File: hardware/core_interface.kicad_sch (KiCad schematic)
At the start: 2 parts, among them J90 Core_LGA, J91 Core_LGA

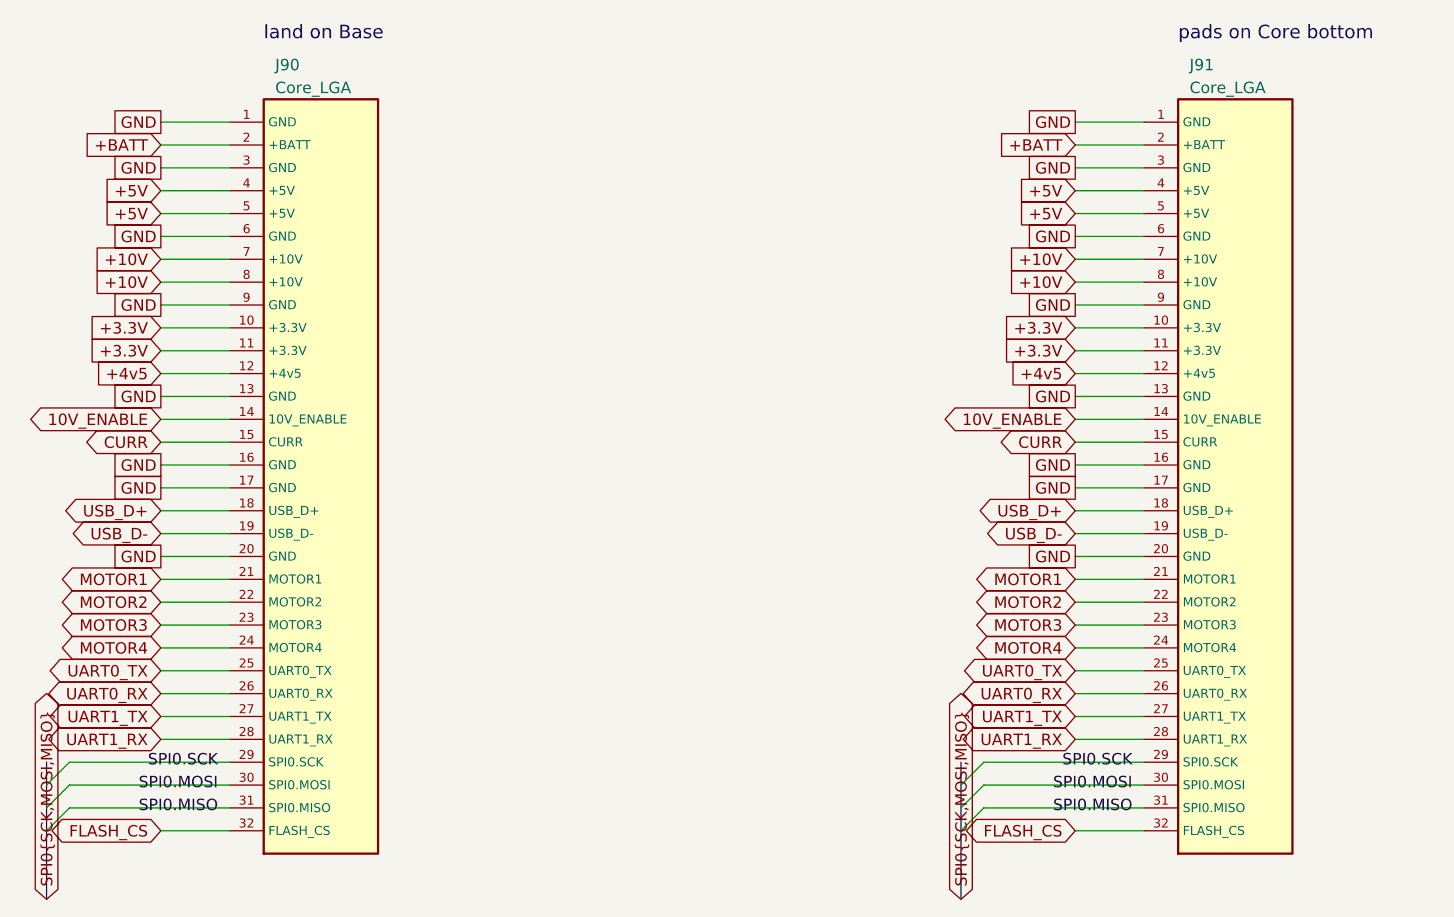
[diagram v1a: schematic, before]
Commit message: OpenAIO: LGA pins from Stan's marker test points, 30 pads, J90/J91 regenerated and placed
lga_gen.py --from-base reads the marker test points on the Base (position +
net) into its pin table and generates footprints, symbol and interface
sheet; lga_apply.py replaces the markers with J90 at the pattern centre and
J91 on the Core, marks the marker symbols exclude-from-board and adds the
LED_STRIP global label on the root (it now crosses the LGA). Plugin update
assigned all 30 pad nets on both boards.

Co-Authored-By: Claude Fable 5 <noreply@anthropic.com>
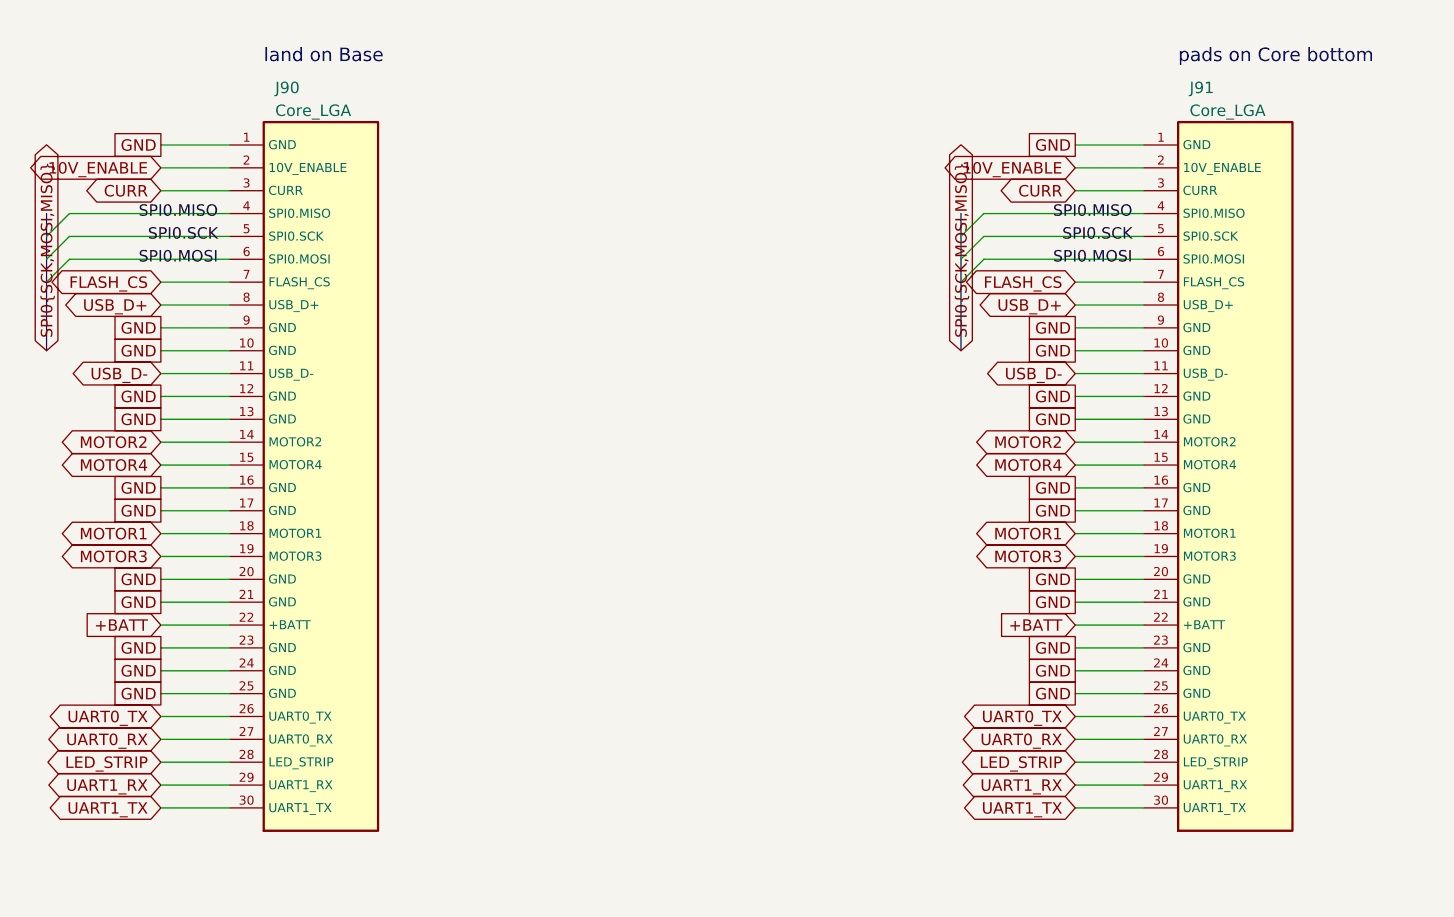
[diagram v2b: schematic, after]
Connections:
- net +4v5 is gone; now on net GND: J90.12 (GND), J91.12 (GND)
- net +BATT: now also J90.22 (+BATT), J91.22 (+BATT); no longer J90.2 (+BATT), J91.2 (+BATT)
- net 10V_ENABLE: now also J90.2 (10V_ENABLE), J91.2 (10V_ENABLE); no longer J90.14 (10V_ENABLE), J91.14 (10V_ENABLE)
- net CURR: now also J90.3 (CURR), J91.3 (CURR); no longer J90.15 (CURR), J91.15 (CURR)
- net FLASH_CS: now also J90.7 (FLASH_CS), J91.7 (FLASH_CS); no longer J90.32 (FLASH_CS), J91.32 (FLASH_CS)
- net GND: now also J90.10 (GND), J90.21 (GND), J90.23 (GND), J90.24 (GND), J90.25 (GND), J91.10 (GND), J91.21 (GND), J91.23 (GND), J91.24 (GND), J91.25 (GND); no longer J90.3 (GND), J90.6 (GND), J91.3 (GND), J91.6 (GND)
- net MOTOR1: now also J90.18 (MOTOR1), J91.18 (MOTOR1); no longer J90.21 (MOTOR1), J91.21 (MOTOR1)
- net MOTOR2: now also J90.14 (MOTOR2), J91.14 (MOTOR2); no longer J90.22 (MOTOR2), J91.22 (MOTOR2)
- net MOTOR3: now also J90.19 (MOTOR3), J91.19 (MOTOR3); no longer J90.23 (MOTOR3), J91.23 (MOTOR3)
- net MOTOR4: now also J90.15 (MOTOR4), J91.15 (MOTOR4); no longer J90.24 (MOTOR4), J91.24 (MOTOR4)
- net SPI0.MISO: now also J90.4 (SPI0.MISO), J91.4 (SPI0.MISO); no longer J90.31 (SPI0.MISO), J91.31 (SPI0.MISO)
- net SPI0.MOSI: now also J90.6 (SPI0.MOSI), J91.6 (SPI0.MOSI); no longer J90.30 (SPI0.MOSI), J91.30 (SPI0.MOSI)
- net SPI0.SCK: now also J90.5 (SPI0.SCK), J91.5 (SPI0.SCK); no longer J90.29 (SPI0.SCK), J91.29 (SPI0.SCK)
- net UART0_RX: now also J90.27 (UART0_RX), J91.27 (UART0_RX); no longer J90.26 (UART0_RX), J91.26 (UART0_RX)
- net UART0_TX: now also J90.26 (UART0_TX), J91.26 (UART0_TX); no longer J90.25 (UART0_TX), J91.25 (UART0_TX)
- net UART1_RX: now also J90.29 (UART1_RX), J91.29 (UART1_RX); no longer J90.28 (UART1_RX), J91.28 (UART1_RX)
- net UART1_TX: now also J90.30 (UART1_TX), J91.30 (UART1_TX); no longer J90.27 (UART1_TX), J91.27 (UART1_TX)
- net USB_D+: now also J90.8 (USB_D+), J91.8 (USB_D+); no longer J90.18 (USB_D+), J91.18 (USB_D+)
- net USB_D-: now also J90.11 (USB_D-), J91.11 (USB_D-); no longer J90.19 (USB_D-), J91.19 (USB_D-)
- removed net +10V: J90.7 (+10V), J90.8 (+10V), J91.7 (+10V), J91.8 (+10V)
- removed net +3.3V: J90.10 (+3.3V), J90.11 (+3.3V), J91.10 (+3.3V), J91.11 (+3.3V)
- removed net +5V: J90.4 (+5V), J90.5 (+5V), J91.4 (+5V), J91.5 (+5V)
- new net LED_STRIP: J90.28 (LED_STRIP), J91.28 (LED_STRIP)
